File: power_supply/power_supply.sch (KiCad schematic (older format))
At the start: 45 parts, among them J1 Conn_01x04_Male, J2 Conn_01x03_Male, J3 Conn_01x03_Male, J4 Conn_01x03_Male, U1 LM7815_TO220, U2 LM7915_TO220, U3 LM7805_TO220

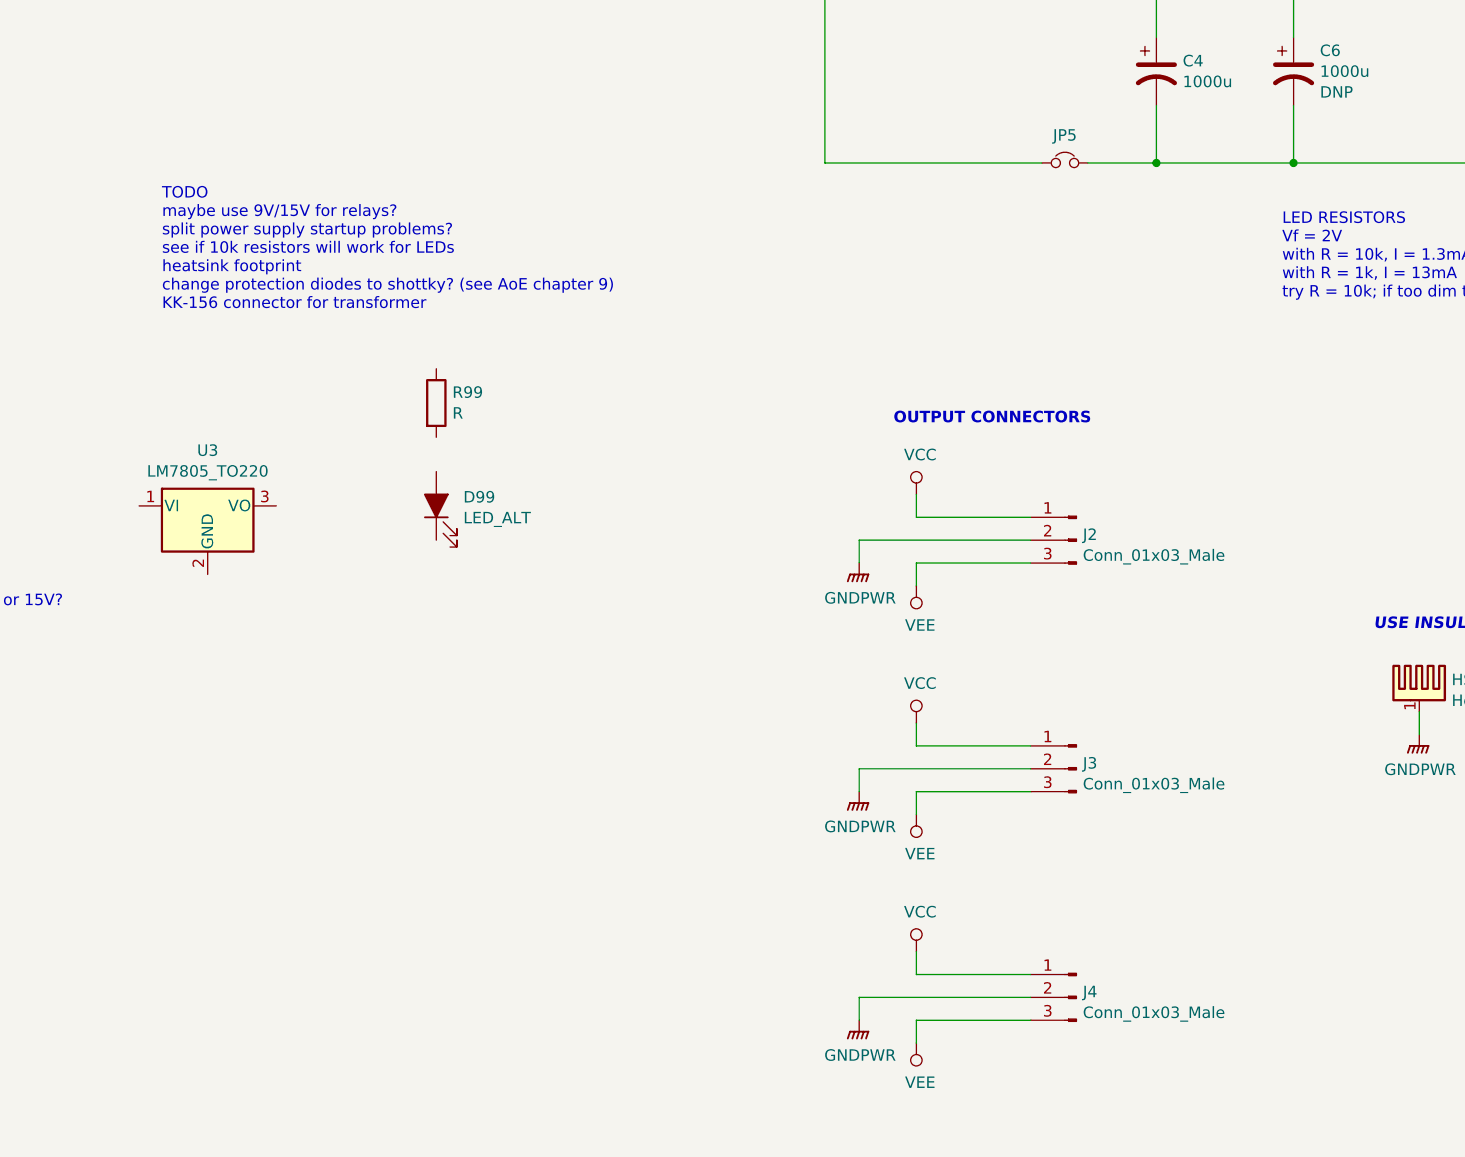
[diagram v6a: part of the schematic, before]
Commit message: redraw output connectors on power supply
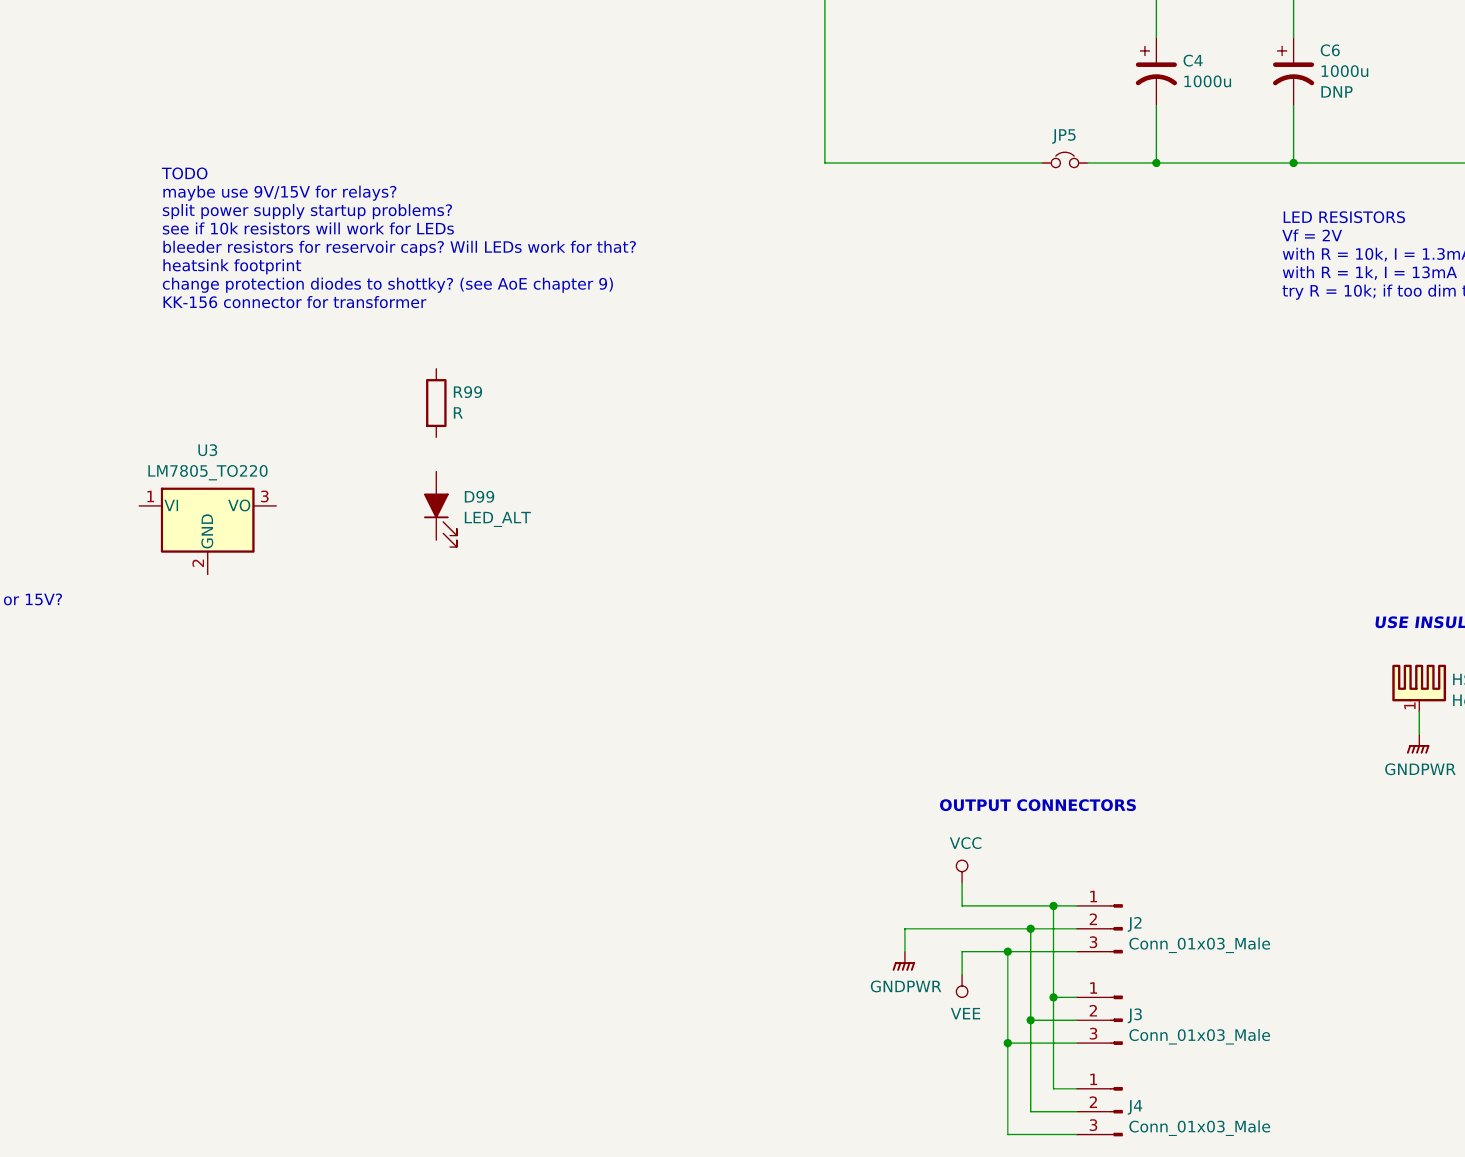
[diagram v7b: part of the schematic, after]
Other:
- note added: "TODO\nmaybe use 9V/15V for relays?\nsplit power supply startup problems?\nsee if 10k resistors will work for LEDs\nbleeder resistors for reservoir caps? Will LEDs work for that?\nheatsink footprint\nchange protection diodes to shottky? (see AoE chapter 9)\nKK-156 connector for transformer"
- note removed: "TODO\nmaybe use 9V/15V for relays?\nsplit power supply startup problems?\nsee if 10k resistors will work for LEDs\nheatsink footprint\nchange protection diodes to shottky? (see AoE chapter 9)\nKK-156 connector for transformer"
- moved on the sheet: J2, J3, J4
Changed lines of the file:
@@
 L Connector:Conn_01x03_Male J2
 U 1 1 5CA83316
-P 4950 5250
-F 0 "J2" H 4922 5274 50  0000 R CNN
-F 1 "Conn_01x03_Male" H 4922 5183 50  0000 R CNN
-F 2 "Connector_Molex_SL:Molex_SL_A-70543-0002_1x03_P2.54mm_Vertical" H 4950 5250 50  0001 C CNN
-F 3 "~" H 4950 5250 50  0001 C CNN
-	1    4950 5250
+P 5150 6950
+F 0 "J2" H 5122 6974 50  0000 R CNN
+F 1 "Conn_01x03_Male" H 5122 6883 50  0000 R CNN
+F 2 "Connector_Molex_SL:Molex_SL_A-70543-0002_1x03_P2.54mm_Vertical" H 5150 6950 50  0001 C CNN
+F 3 "~" H 5150 6950 50  0001 C CNN
+	1    5150 6950
 	-1   0    0    -1
 $EndComp
@@
 L Connector:Conn_01x03_Male J3
 U 1 1 5CA83A0D
-P 4950 6250
-F 0 "J3" H 4922 6274 50  0000 R CNN
-F 1 "Conn_01x03_Male" H 4922 6183 50  0000 R CNN
-F 2 "Connector_Molex_SL:Molex_SL_A-70543-0002_1x03_P2.54mm_Vertical" H 4950 6250 50  0001 C CNN
-F 3 "~" H 4950 6250 50  0001 C CNN
-	1    4950 6250
+P 5150 7350
+F 0 "J3" H 5122 7374 50  0000 R CNN
+F 1 "Conn_01x03_Male" H 5122 7283 50  0000 R CNN
+F 2 "Connector_Molex_SL:Molex_SL_A-70543-0002_1x03_P2.54mm_Vertical" H 5150 7350 50  0001 C CNN
+F 3 "~" H 5150 7350 50  0001 C CNN
+	1    5150 7350
 	-1   0    0    -1
 $EndComp
@@
 L Connector:Conn_01x03_Male J4
 U 1 1 5CA83D7D
-P 4950 7250
-F 0 "J4" H 4922 7274 50  0000 R CNN
-F 1 "Conn_01x03_Male" H 4922 7183 50  0000 R CNN
-F 2 "Connector_Molex_SL:Molex_SL_A-70543-0002_1x03_P2.54mm_Vertical" H 4950 7250 50  0001 C CNN
-F 3 "~" H 4950 7250 50  0001 C CNN
-	1    4950 7250
+P 5150 7750
+F 0 "J4" H 5122 7774 50  0000 R CNN
+F 1 "Conn_01x03_Male" H 5122 7683 50  0000 R CNN
+F 2 "Connector_Molex_SL:Molex_SL_A-70543-0002_1x03_P2.54mm_Vertical" H 5150 7750 50  0001 C CNN
+F 3 "~" H 5150 7750 50  0001 C CNN
+	1    5150 7750
 	-1   0    0    -1
 $EndComp
-Wire Wire Line
-	4250 7150 4750 7150
-Wire Wire Line
-	4250 7350 4750 7350
-$Comp
-L power:VCC #PWR0108
-U 1 1 5CA96434
-P 4250 7050
-F 0 "#PWR0108" H 4250 6900 50  0001 C CNN
-F 1 "VCC" H 4267 7223 50  0000 C CNN
-F 2 "" H 4250 7050 50  0001 C CNN
-F 3 "" H 4250 7050 50  0001 C CNN
-	1    4250 7050
-	1    0    0    -1
-$EndComp
-$Comp
-L power:VEE #PWR0109
-U 1 1 5CA96ADA
-P 4250 7450
-F 0 "#PWR0109" H 4250 7300 50  0001 C CNN
-F 1 "VEE" H 4267 7623 50  0000 C CNN
-F 2 "" H 4250 7450 50  0001 C CNN
-F 3 "" H 4250 7450 50  0001 C CNN
-	1    4250 7450
-	1    0    0    1
-$EndComp
-Wire Wire Line
-	4250 7050 4250 7150
-Wire Wire Line
-	4250 7350 4250 7450
-$Comp
-L power:GNDPWR #PWR0110
-U 1 1 5CA9D8F5
-P 4000 7350
-F 0 "#PWR0110" H 4000 7150 50  0001 C CNN
-F 1 "GNDPWR" H 4004 7196 50  0000 C CNN
-F 2 "" H 4000 7300 50  0001 C CNN
-F 3 "" H 4000 7300 50  0001 C CNN
-	1    4000 7350
-	1    0    0    -1
-$EndComp
-Wire Wire Line
-	4000 7350 4000 7250
-Wire Wire Line
-	4000 7250 4750 7250
 $Comp
 L power:VCC #PWR0111
 U 1 1 5CAA4ADE
-P 4250 5050
-F 0 "#PWR0111" H 4250 4900 50  0001 C CNN
-F 1 "VCC" H 4267 5223 50  0000 C CNN
-F 2 "" H 4250 5050 50  0001 C CNN
-F 3 "" H 4250 5050 50  0001 C CNN
-	1    4250 5050
+P 4450 6750
+F 0 "#PWR0111" H 4450 6600 50  0001 C CNN
+F 1 "VCC" H 4467 6923 50  0000 C CNN
+F 2 "" H 4450 6750 50  0001 C CNN
+F 3 "" H 4450 6750 50  0001 C CNN
+	1    4450 6750
 	1    0    0    -1
 $EndComp
@@
 L power:VEE #PWR0112
 U 1 1 5CAA4AE4
-P 4250 5450
-F 0 "#PWR0112" H 4250 5300 50  0001 C CNN
-F 1 "VEE" H 4267 5623 50  0000 C CNN
-F 2 "" H 4250 5450 50  0001 C CNN
-F 3 "" H 4250 5450 50  0001 C CNN
-	1    4250 5450
+P 4450 7150
+F 0 "#PWR0112" H 4450 7000 50  0001 C CNN
+F 1 "VEE" H 4467 7323 50  0000 C CNN
+F 2 "" H 4450 7150 50  0001 C CNN
+F 3 "" H 4450 7150 50  0001 C CNN
+	1    4450 7150
 	1    0    0    1
 $EndComp
 Wire Wire Line
-	4250 5050 4250 5150
-Wire Wire Line
-	4250 5350 4250 5450
+	4450 6750 4450 6850
+Wire Wire Line
+	4450 7050 4450 7150
 $Comp
 L power:GNDPWR #PWR0113
 U 1 1 5CAA4AEC
-P 4000 5350
-F 0 "#PWR0113" H 4000 5150 50  0001 C CNN
-F 1 "GNDPWR" H 4004 5196 50  0000 C CNN
-F 2 "" H 4000 5300 50  0001 C CNN
-F 3 "" H 4000 5300 50  0001 C CNN
-	1    4000 5350
-	1    0    0    -1
-$EndComp
-Wire Wire Line
-	4000 5350 4000 5250
-Wire Wire Line
-	4250 6150 4750 6150
-Wire Wire Line
-	4250 6350 4750 6350
-$Comp
-L power:VCC #PWR0114
-U 1 1 5CAD22F2
-P 4250 6050
-F 0 "#PWR0114" H 4250 5900 50  0001 C CNN
-F 1 "VCC" H 4267 6223 50  0000 C CNN
-F 2 "" H 4250 6050 50  0001 C CNN
-F 3 "" H 4250 6050 50  0001 C CNN
-	1    4250 6050
-	1    0    0    -1
-$EndComp
-$Comp
-L power:VEE #PWR0115
-U 1 1 5CAD22F8
-P 4250 6450
-F 0 "#PWR0115" H 4250 6300 50  0001 C CNN
-F 1 "VEE" H 4267 6623 50  0000 C CNN
-F 2 "" H 4250 6450 50  0001 C CNN
-F 3 "" H 4250 6450 50  0001 C CNN
-	1    4250 6450
-	1    0    0    1
-$EndComp
-Wire Wire Line
-	4250 6050 4250 6150
-Wire Wire Line
-	4250 6350 4250 6450
-$Comp
-L power:GNDPWR #PWR0116
-U 1 1 5CAD2300
-P 4000 6350
-F 0 "#PWR0116" H 4000 6150 50  0001 C CNN
-F 1 "GNDPWR" H 4004 6196 50  0000 C CNN
-F 2 "" H 4000 6300 50  0001 C CNN
-F 3 "" H 4000 6300 50  0001 C CNN
-	1    4000 6350
-	1    0    0    -1
-$EndComp
-Wire Wire Line
-	4000 6350 4000 6250
-Wire Wire Line
-	4000 6250 4750 6250
-Wire Wire Line
-	4250 5150 4750 5150
-Wire Wire Line
-	4250 5350 4750 5350
-Wire Wire Line
-	4000 5250 4750 5250
+P 4200 7050
+F 0 "#PWR0113" H 4200 6850 50  0001 C CNN
+F 1 "GNDPWR" H 4204 6896 50  0000 C CNN
+F 2 "" H 4200 7000 50  0001 C CNN
+F 3 "" H 4200 7000 50  0001 C CNN
+	1    4200 7050
+	1    0    0    -1
+$EndComp
+Wire Wire Line
+	4200 7050 4200 6950
 Wire Wire Line
 	1900 1550 1900 2650
@@
 $EndComp
 Text Notes 950  4250 0    50   ~ 0
-TODO\nmaybe use 9V/15V for relays?\nsplit power supply startup problems?\nsee if 10k resistors will work for LEDs\nheatsink footprint\nchange protection diodes to shottky? (see AoE chapter 9)\nKK-156 connector for transformer
+TODO\nmaybe use 9V/15V for relays?\nsplit power supply startup problems?\nsee if 10k resistors will work for LEDs\nbleeder resistors for reservoir caps? Will LEDs work for that?\nheatsink footprint\nchange protection diodes to shottky? (see AoE chapter 9)\nKK-156 connector for transformer
 $Comp
 L Device:CP1 C8
@@
 Wire Wire Line
 	7450 3600 7550 3600
-Text Notes 4150 4750 0    50   ~ 10
+Text Notes 4350 6450 0    50   ~ 10
 OUTPUT CONNECTORS
 Text Notes 950  1750 0    50   ~ 10
@@
 Text Notes 6250 5650 0    50   Italic 10
 USE INSULATING PADS FOR HEATSINKS
+Wire Wire Line
+	4450 7050 4650 7050
+Wire Wire Line
+	4200 6950 4750 6950
+Wire Wire Line
+	4450 6850 4850 6850
+Wire Wire Line
+	4950 7250 4850 7250
+Wire Wire Line
+	4850 7250 4850 6850
+Connection ~ 4850 6850
+Wire Wire Line
+	4850 6850 4950 6850
+Wire Wire Line
+	4850 7250 4850 7650
+Wire Wire Line
+	4850 7650 4950 7650
+Connection ~ 4850 7250
+Wire Wire Line
+	4950 7350 4750 7350
+Wire Wire Line
+	4750 7350 4750 6950
+Connection ~ 4750 6950
+Wire Wire Line
+	4750 6950 4950 6950
+Wire Wire Line
+	4750 7350 4750 7750
+Wire Wire Line
+	4750 7750 4950 7750
+Connection ~ 4750 7350
+Wire Wire Line
+	4650 7850 4650 7450
+Connection ~ 4650 7050
+Wire Wire Line
+	4650 7050 4950 7050
+Wire Wire Line
+	4950 7450 4650 7450
+Connection ~ 4650 7450
+Wire Wire Line
+	4650 7450 4650 7050
+Wire Wire Line
+	4650 7850 4950 7850
 $EndSCHEMATC
